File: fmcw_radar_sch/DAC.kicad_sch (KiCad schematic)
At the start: 15 parts, among them U400 DAC7563SDGSR, U401 MCP6001T-E/OT

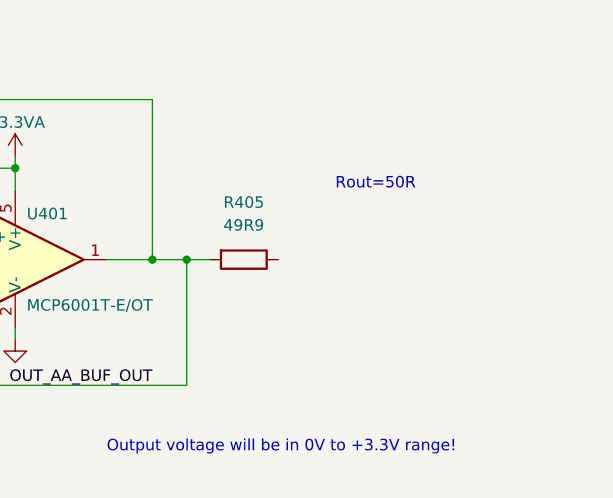
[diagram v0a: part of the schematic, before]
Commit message: Layout of controller board
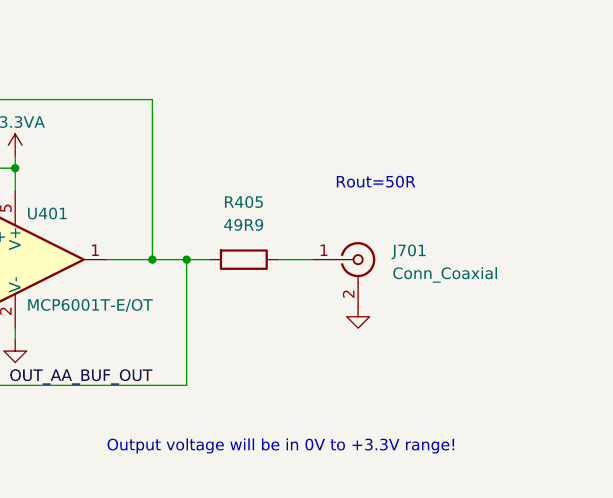
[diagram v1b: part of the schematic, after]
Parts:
- added J701: Conn_Coaxial, Connector_Coaxial:BNC_Amphenol_031-5539_Vertical, symbol Connector:Conn_Coaxial
- U400: footprint PhilsLab_Footprints_KiCad6:VSSOP-10 -> nonkicad:DGS0010A_L
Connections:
- net GND: now also J701.2 (Ext)
- net at R405.1: now also J701.1 (In)
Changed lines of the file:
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@@
+	(wire
+		(pts
+			(xy 231.14 59.69) (xy 227.33 59.69)
+		)
+		(stroke
+			(width 0)
+			(type default)
+		)
+	)
 	(wire
 		(pts
@@
 			)
 		)
-		(property "Footprint" "PhilsLab_Footprints_KiCad6:VSSOP-10"
+		(property "Footprint" "nonkicad:DGS0010A_L"
 			(at 93.98 69.85 0)
 			(effects
@@
 					(unit 1)
 				)
+			)
+		)
+	)
+	(symbol
+		(lib_id "power:GND")
+		(at 236.22 64.77 0)
+		(unit 1)
+		(exclude_from_sim no)
+		(in_bom yes)
+		(on_board yes)
+		(dnp no)
+		(property "Reference" "#PWR0701"
+			(at 236.22 71.12 0)
+			(effects
+				(font
+					(size 1.27 1.27)
+				)
+				(hide yes)
+			)
+		)
+		(property "Value" "GND"
+			(at 236.22 68.58 0)
+			(effects
+				(font
+					(size 1.27 1.27)
+				)
+				(hide yes)
+			)
+		)
+		(property "Footprint" ""
+			(at 236.22 64.77 0)
+			(effects
+				(font
+					(size 1.27 1.27)
+				)
+				(hide yes)
+			)
+		)
+		(property "Datasheet" ""
+			(at 236.22 64.77 0)
+			(effects
+				(font
+					(size 1.27 1.27)
+				)
+				(hide yes)
+			)
+		)
+		(property "Description" ""
+			(at 236.22 64.77 0)
+			(effects
+				(font
+					(size 1.27 1.27)
+				)
+			)
+		)
+		(pin "1"
+		)
+		(instances
+			(project "fmcw_radar_sch"
+				(path "/435eb955-ea36-4ca2-96a0-71f0d07942fb/30da698b-30e2-4529-9d15-1e8bb80cecea"
+					(reference "#PWR0701")
+					(unit 1)
+				)
+			)
+		)
+	)
+	(symbol
+		(lib_id "Connector:Conn_Coaxial")
+		(at 236.22 59.69 0)
+		(unit 1)
+		(exclude_from_sim no)
+		(in_bom yes)
+		(on_board yes)
+		(dnp no)
+		(fields_autoplaced yes)
+		(property "Reference" "J701"
+			(at 240.03 58.7131 0)
+			(effects
+				(font
+					(size 1.27 1.27)
+				)
+				(justify left)
+			)
+		)
+		(property "Value" "Conn_Coaxial"
+			(at 240.03 61.2531 0)
+			(effects
+				(font
+					(size 1.27 1.27)
+				)
+				(justify left)
+			)
+		)
+		(property "Footprint" "Connector_Coaxial:BNC_Amphenol_031-5539_Vertical"
+			(at 236.22 59.69 0)
+			(effects
+				(font
+					(size 1.27 1.27)
+				)
+				(hide yes)
+			)
+		)
+		(property "Datasheet" "~"
+			(at 236.22 59.69 0)
+			(effects
+				(font
+					(size 1.27 1.27)
+				)
+				(hide yes)
+			)
+		)
+		(property "Description" "coaxial connector (BNC, SMA, SMB, SMC, Cinch/RCA, LEMO, ...)"
+			(at 236.22 59.69 0)
+			(effects
+				(font
+					(size 1.27 1.27)
+				)
+				(hide yes)
+			)
+		)
+		(pin "2"
+		)
+		(pin "1"
+		)
+		(instances
+			(project ""
+				(path "/435eb955-ea36-4ca2-96a0-71f0d07942fb/30da698b-30e2-4529-9d15-1e8bb80cecea"
+					(reference "J701")
+					(unit 1)
+				)

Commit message: CHANGES
changes
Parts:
- renumbered C400 to C37, C401 to C38, C402 to C39, C403 to C40, C405 to C41, C404 to C42, C406 to C43, J701 to J11, R400 to R19, R401 to R20, R402 to R21, R403 to R22, R404 to R23, R405 to R24, U401 to U10, U400 to U9
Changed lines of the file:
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@@
 		(on_board yes)
 		(dnp no)
-		(property "Reference" "R400"
+		(property "Reference" "R19"
 			(at 63.5 58.42 90)
 			(effects
@@
 			(project "fmcw_radar_sch"
 				(path "/435eb955-ea36-4ca2-96a0-71f0d07942fb/30da698b-30e2-4529-9d15-1e8bb80cecea"
-					(reference "R400")
+					(reference "R19")
 					(unit 1)
 				)
@@
 		(on_board yes)
 		(dnp no)
-		(property "Reference" "#PWR060"
+		(property "Reference" "#PWR070"
 			(at 68.58 39.37 0)
 			(effects
@@
 			(project "fmcw_radar_sch"
 				(path "/435eb955-ea36-4ca2-96a0-71f0d07942fb/30da698b-30e2-4529-9d15-1e8bb80cecea"
-					(reference "#PWR060")
+					(reference "#PWR070")
 					(unit 1)
 				)
@@
 		(on_board yes)
 		(dnp no)
-		(property "Reference" "#PWR068"
+		(property "Reference" "#PWR072"
 			(at 93.98 87.63 0)
 			(effects
@@
 			(project "fmcw_radar_sch"
 				(path "/435eb955-ea36-4ca2-96a0-71f0d07942fb/30da698b-30e2-4529-9d15-1e8bb80cecea"
-					(reference "#PWR068")
+					(reference "#PWR072")
 					(unit 1)
 				)
@@
 		(on_board yes)
 		(dnp no)
-		(property "Reference" "C402"
+		(property "Reference" "C39"
 			(at 123.19 72.39 0)
 			(effects
@@
 			(project "fmcw_radar_sch"
 				(path "/435eb955-ea36-4ca2-96a0-71f0d07942fb/30da698b-30e2-4529-9d15-1e8bb80cecea"
-					(reference "C402")
+					(reference "C39")
 					(unit 1)
 				)
@@
 		(on_board yes)
 		(dnp no)
-		(property "Reference" "C400"
+		(property "Reference" "C37"
 			(at 72.39 40.64 0)
 			(effects
@@
 			(project "fmcw_radar_sch"
 				(path "/435eb955-ea36-4ca2-96a0-71f0d07942fb/30da698b-30e2-4529-9d15-1e8bb80cecea"
-					(reference "C400")
+					(reference "C37")
 					(unit 1)
 				)
@@
 		(on_board yes)
 		(dnp no)
-		(property "Reference" "U400"
+		(property "Reference" "U9"
 			(at 104.14 52.07 0)
 			(effects
@@
 			(project "fmcw_radar_sch"
 				(path "/435eb955-ea36-4ca2-96a0-71f0d07942fb/30da698b-30e2-4529-9d15-1e8bb80cecea"
-					(reference "U400")
+					(reference "U9")
 					(unit 1)
 				)
@@
 		(on_board yes)
 		(dnp no)
-		(property "Reference" "C401"
+		(property "Reference" "C38"
 			(at 85.09 40.64 0)
 			(effects
@@
 			(project "fmcw_radar_sch"
 				(path "/435eb955-ea36-4ca2-96a0-71f0d07942fb/30da698b-30e2-4529-9d15-1e8bb80cecea"
-					(reference "C401")
+					(reference "C38")
 					(unit 1)
 				)
@@
 		(on_board yes)
 		(dnp no)
-		(property "Reference" "#PWR061"
+		(property "Reference" "#PWR071"
 			(at 68.58 54.61 0)
 			(effects
@@
 			(project "fmcw_radar_sch"
 				(path "/435eb955-ea36-4ca2-96a0-71f0d07942fb/30da698b-30e2-4529-9d15-1e8bb80cecea"
-					(reference "#PWR061")
+					(reference "#PWR071")
 					(unit 1)
 				)
@@
 		(on_board yes)
 		(dnp no)
-		(property "Reference" "R401"
+		(property "Reference" "R20"
 			(at 134.62 72.39 0)
 			(effects
@@
 			(project "fmcw_radar_sch"
 				(path "/435eb955-ea36-4ca2-96a0-71f0d07942fb/30da698b-30e2-4529-9d15-1e8bb80cecea"
-					(reference "R401")
+					(reference "R20")
 					(unit 1)
 				)
@@
 		(on_board yes)
 		(dnp no)
-		(property "Reference" "U401"
+		(property "Reference" "U10"
 			(at 199.39 54.61 0)
 			(effects
@@
 			(project "fmcw_radar_sch"
 				(path "/435eb955-ea36-4ca2-96a0-71f0d07942fb/30da698b-30e2-4529-9d15-1e8bb80cecea"
-					(reference "U401")
+					(reference "U10")
 					(unit 1)
 				)
@@
 		(on_board yes)
 		(dnp no)
-		(property "Reference" "C406"
+		(property "Reference" "C43"
 			(at 185.42 45.72 90)
 			(effects
@@
 			(project "fmcw_radar_sch"
 				(path "/435eb955-ea36-4ca2-96a0-71f0d07942fb/30da698b-30e2-4529-9d15-1e8bb80cecea"
-					(reference "C406")
+					(reference "C43")
 					(unit 1)
 				)
@@
 		(on_board yes)
 		(dnp no)
-		(property "Reference" "#PWR064"
+		(property "Reference" "#PWR077"
 			(at 198.12 74.93 0)
 			(effects
@@
 			(project "fmcw_radar_sch"
 				(path "/435eb955-ea36-4ca2-96a0-71f0d07942fb/30da698b-30e2-4529-9d15-1e8bb80cecea"
-					(reference "#PWR064")
+					(reference "#PWR077")
 					(unit 1)
 				)
@@
 		(on_board yes)
 		(dnp no)
-		(property "Reference" "#PWR063"
+		(property "Reference" "#PWR075"
 			(at 181.61 55.88 0)
 			(effects
@@
 			(project "fmcw_radar_sch"
 				(path "/435eb955-ea36-4ca2-96a0-71f0d07942fb/30da698b-30e2-4529-9d15-1e8bb80cecea"
-					(reference "#PWR063")
+					(reference "#PWR075")
 					(unit 1)
 				)
@@
 		(on_board yes)
 		(dnp no)
-		(property "Reference" "R402"
+		(property "Reference" "R21"
 			(at 140.97 50.8 90)
 			(effects
@@
 			(project "fmcw_radar_sch"
 				(path "/435eb955-ea36-4ca2-96a0-71f0d07942fb/30da698b-30e2-4529-9d15-1e8bb80cecea"
-					(reference "R402")
+					(reference "R21")
 					(unit 1)
 				)
@@
 		(on_board yes)
 		(dnp no)
-		(property "Reference" "C403"
+		(property "Reference" "C40"
 			(at 151.13 62.23 0)
 			(effects
@@
 			(project "fmcw_radar_sch"
 				(path "/435eb955-ea36-4ca2-96a0-71f0d07942fb/30da698b-30e2-4529-9d15-1e8bb80cecea"
-					(reference "C403")
+					(reference "C40")
 					(unit 1)
 				)
@@
 		(on_board yes)
 		(dnp no)
-		(property "Reference" "R403"
+		(property "Reference" "R22"
 			(at 153.67 50.8 90)
 			(effects
@@
 			(project "fmcw_radar_sch"
 				(path "/435eb955-ea36-4ca2-96a0-71f0d07942fb/30da698b-30e2-4529-9d15-1e8bb80cecea"
-					(reference "R403")
+					(reference "R22")
 					(unit 1)
 				)
@@
 		(on_board yes)
 		(dnp no)
-		(property "Reference" "#PWR065"
+		(property "Reference" "#PWR073"
 			(at 147.32 76.2 0)
 			(effects
@@
 			(project "fmcw_radar_sch"
 				(path "/435eb955-ea36-4ca2-96a0-71f0d07942fb/30da698b-30e2-4529-9d15-1e8bb80cecea"
-					(reference "#PWR065")
+					(reference "#PWR073")
 					(unit 1)
 				)
@@
 		(on_board yes)
 		(dnp no)
-		(property "Reference" "R404"
+		(property "Reference" "R23"
 			(at 166.37 50.8 90)
 			(effects
@@
 			(project "fmcw_radar_sch"
 				(path "/435eb955-ea36-4ca2-96a0-71f0d07942fb/30da698b-30e2-4529-9d15-1e8bb80cecea"
-					(reference "R404")
+					(reference "R23")
 					(unit 1)
 				)
@@
 		(on_board yes)
 		(dnp no)
-		(property "Reference" "C404"
+		(property "Reference" "C42"
 			(at 176.53 62.23 0)
 			(effects
@@
 			(project "fmcw_radar_sch"
 				(path "/435eb955-ea36-4ca2-96a0-71f0d07942fb/30da698b-30e2-4529-9d15-1e8bb80cecea"
-					(reference "C404")
+					(reference "C42")
 					(unit 1)
 				)
@@
 		(on_board yes)
 		(dnp no)
-		(property "Reference" "R405"
+		(property "Reference" "R24"
 			(at 223.52 53.34 90)
 			(effects
@@
 			(project "fmcw_radar_sch"
 				(path "/435eb955-ea36-4ca2-96a0-71f0d07942fb/30da698b-30e2-4529-9d15-1e8bb80cecea"
-					(reference "R405")
+					(reference "R24")
 					(unit 1)
 				)
@@
 		(on_board yes)
 		(dnp no)
-		(property "Reference" "#PWR066"
+		(property "Reference" "#PWR074"
 			(at 172.72 76.2 0)
 			(effects
@@
 			(project "fmcw_radar_sch"
 				(path "/435eb955-ea36-4ca2-96a0-71f0d07942fb/30da698b-30e2-4529-9d15-1e8bb80cecea"
-					(reference "#PWR066")
+					(reference "#PWR074")
 					(unit 1)
 				)
@@
 		(on_board yes)
 		(dnp no)
-		(property "Reference" "#PWR062"
+		(property "Reference" "#PWR076"
 			(at 198.12 52.07 0)
 			(effects
@@
 			(project "fmcw_radar_sch"
 				(path "/435eb955-ea36-4ca2-96a0-71f0d07942fb/30da698b-30e2-4529-9d15-1e8bb80cecea"
-					(reference "#PWR062")
+					(reference "#PWR076")
 					(unit 1)
 				)
@@
 		(on_board yes)
 		(dnp no)
-		(property "Reference" "C405"
+		(property "Reference" "C41"
 			(at 175.26 38.1 90)
 			(effects
@@
 			(project "fmcw_radar_sch"
 				(path "/435eb955-ea36-4ca2-96a0-71f0d07942fb/30da698b-30e2-4529-9d15-1e8bb80cecea"
-					(reference "C405")
+					(reference "C41")
 					(unit 1)
 				)
@@
 		(on_board yes)
 		(dnp no)
-		(property "Reference" "#PWR0701"
+		(property "Reference" "#PWR078"
 			(at 236.22 71.12 0)
 			(effects
@@
 			(project "fmcw_radar_sch"
 				(path "/435eb955-ea36-4ca2-96a0-71f0d07942fb/30da698b-30e2-4529-9d15-1e8bb80cecea"
-					(reference "#PWR0701")
+					(reference "#PWR078")
 					(unit 1)
 				)
@@
 		(dnp no)
 		(fields_autoplaced yes)
-		(property "Reference" "J701"
+		(property "Reference" "J11"
 			(at 240.03 58.7131 0)
 			(effects
@@
 			(project ""
 				(path "/435eb955-ea36-4ca2-96a0-71f0d07942fb/30da698b-30e2-4529-9d15-1e8bb80cecea"
-					(reference "J701")
-					(unit 1)
-				)
+					(reference "J11")
+					(unit 1)
+				)

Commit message: Routing
Routing
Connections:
- net SPI2_MOSI renamed MOSI2
- net SPI2_NSS renamed NSS2
- net SPI2_SCK renamed SCK2
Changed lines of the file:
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@@
+		)
+	)
+	(global_label "MOSI2"
+		(shape input)
+		(at 57.15 57.15 180)
+		(fields_autoplaced yes)
+		(effects
+			(font
+				(size 1.27 1.27)
+			)
+			(justify right)
+		)
+		(property "Intersheetrefs" "${INTERSHEET_REFS}"
+			(at 48.3591 57.15 0)
+			(effects
+				(font
+					(size 1.27 1.27)
+				)
+				(justify right)
+				(hide yes)
+			)
 		)
 	)
@@
 		)
 	)
-	(global_label "SPI2_SCK"
+	(global_label "SCK2"
 		(shape input)
 		(at 57.15 60.96 180)
@@
 		)
 		(property "Intersheetrefs" "${INTERSHEET_REFS}"
-			(at 45.8081 60.96 0)
-			(effects
-				(font
-					(size 1.27 1.27)
-				)
-				(justify right)
-				(hide yes)
-			)
-		)
-	)
-	(global_label "SPI2_NSS"
-		(shape input)
-		(at 57.15 64.77 180)
-		(fields_autoplaced yes)
-		(effects
-			(font
-				(size 1.27 1.27)
-			)
-			(justify right)
-		)
-		(property "Intersheetrefs" "${INTERSHEET_REFS}"
-			(at 45.8081 64.77 0)
-			(effects
-				(font
-					(size 1.27 1.27)
-				)
-				(justify right)
-				(hide yes)
-			)
-		)
-	)
-	(global_label "SPI2_MOSI"
-		(shape input)
-		(at 57.15 57.15 180)
-		(fields_autoplaced yes)
-		(effects
-			(font
-				(size 1.27 1.27)
-			)
-			(justify right)
-		)
-		(property "Intersheetrefs" "${INTERSHEET_REFS}"
-			(at 44.9682 57.0706 0)
+			(at 49.2058 60.96 0)
 			(effects
 				(font
@@
 			(effects
 				(font
+					(size 1.27 1.27)
+				)
+				(justify right)
+				(hide yes)
+			)
+		)
+	)
+	(global_label "NSS2"
+		(shape input)
+		(at 57.15 64.77 180)
+		(fields_autoplaced yes)
+		(effects
+			(font
+				(size 1.27 1.27)
+			)
+			(justify right)
+		)
+		(property "Intersheetrefs" "${INTERSHEET_REFS}"
+			(at 49.2058 64.77 0)
+			(effects
+				(font
